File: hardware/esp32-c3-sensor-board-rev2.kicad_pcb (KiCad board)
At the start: 2 copper layers, 46 x 89 mm, 14 parts, among them J1 BME280_Module, J2 BH1750_Module, J3 Relay, J4 Button, J5 BREAKOUT, U1 ESP32-C3-SuperMini, U2 HLK-LD2410C

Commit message: Fix ESP32-C3 Super Mini pinout and re-route rev2
- Correct the U1 socket footprint pad order to match the physical module
  (pad 1 = 5V at the USB end, pad 8 = GPIO0, pad 9 = GPIO5, pad 16 = GPIO21).
- Use the reference pinout for I2C: SDA = GPIO8, SCL = GPIO9; free GPIO6/7
  go to the J5 breakout row. UART stays GPIO20/21, relay GPIO4, button GPIO3.
- Add full pin descriptions to the ESP32 symbol and board silkscreen
  (GPIOx plus MISO/MOSI/SS/SDA/SCL/RX/TX), and update all docs.
- Re-route the board against the corrected pin order (FreeRouting);
  DRC 0 errors / 0 unconnected, 2 pre-existing cosmetic silk warnings.
- Regenerate gerbers, drill, job file and the gerber zip.

doorbell.yml still lists GPIO6/7 for I2C and must be updated to
sda: GPIO8 / scl: GPIO9 on the software side.

Co-Authored-By: Claude Code <noreply@anthropic.com>
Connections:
- J5 pad 8: IO8 -> IO6
- J5 pad 9: IO9 -> IO7
- U1 pad 10: I2C_SDA -> IO6
- U1 pad 11: I2C_SCL -> IO7
- U1 pad 12: IO8 -> I2C_SDA
- U1 pad 13: IO9 -> I2C_SCL
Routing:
- net IO9: track 58.6 -> 0.00 mm
- net IO6: track 0.00 -> 52.1 mm
- net IO8: track 50.9 -> 0.00 mm
- net IO7: track 0.00 -> 49.9 mm, vias 0 -> 2
- net UART_RX: track 95.1 -> 62.2 mm, vias 0 -> 1
- net SPI_CS: track 86.1 -> 108.6 mm
- net I2C_SCL: track 71.7 -> 93.5 mm, vias 1 -> 0
- net 5V: track 67.6 -> 88.8 mm, vias 0 -> 1
- net IO0: track 34.6 -> 17.2 mm
- net UART_TX: track 74.5 -> 89.5 mm
- net 3V3: track 77.2 -> 90.9 mm
- net BUTTON: track 25.0 -> 36.8 mm
- net IO1: track 34.6 -> 24.1 mm
- net IO2: track 34.6 -> 27.3 mm, vias 0 -> 1
- net I2C_SDA: track 66.9 -> 73.3 mm, vias 1 -> 0
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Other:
- board text added: "GPIO0"
- board text added: "GPIO1"
- board text added: "GPIO10"
- board text added: "GPIO10 GPIO20=RX GPIO21=TX"
- board text added: "GPIO2"
- board text added: "GPIO20"
- board text added: "GPIO21"
- board text added: "GPIO4"
- board text added: "GPIO5"
- board text added: "GPIO6"
- board text added: "GPIO7"
- board text added: "GPIO7=SS GPIO8=SDA GPIO9=SCL"
- board text added: "GPIO8"
- board text added: "GPIO9"
- board text added: "JP1 1-2=I2C CSB->3V3 | 2-3=SPI CSB->GPIO5"
- board text added: "JP2 1-2=I2C 0x76 SDO->GND | 2-3=SPI MISO GPIO10"
- board text added: "U1 ALT: GPIO5=MISO GPIO6=MOSI"
- board text removed: "BTN"
- board text removed: "IO0"
- board text removed: "IO1"
- board text removed: "IO10"
- board text removed: "IO2"
- board text removed: "IO5"
- board text removed: "IO8"
- board text removed: "IO9"
- board text removed: "JP1 1-2=I2C CSB->3V3 | 2-3=SPI CSB->IO5"
- board text removed: "JP2 1-2=I2C 0x76 SDO->GND | 2-3=SPI MISO IO10"
- board text removed: "NC"
- board text removed: "RLY"

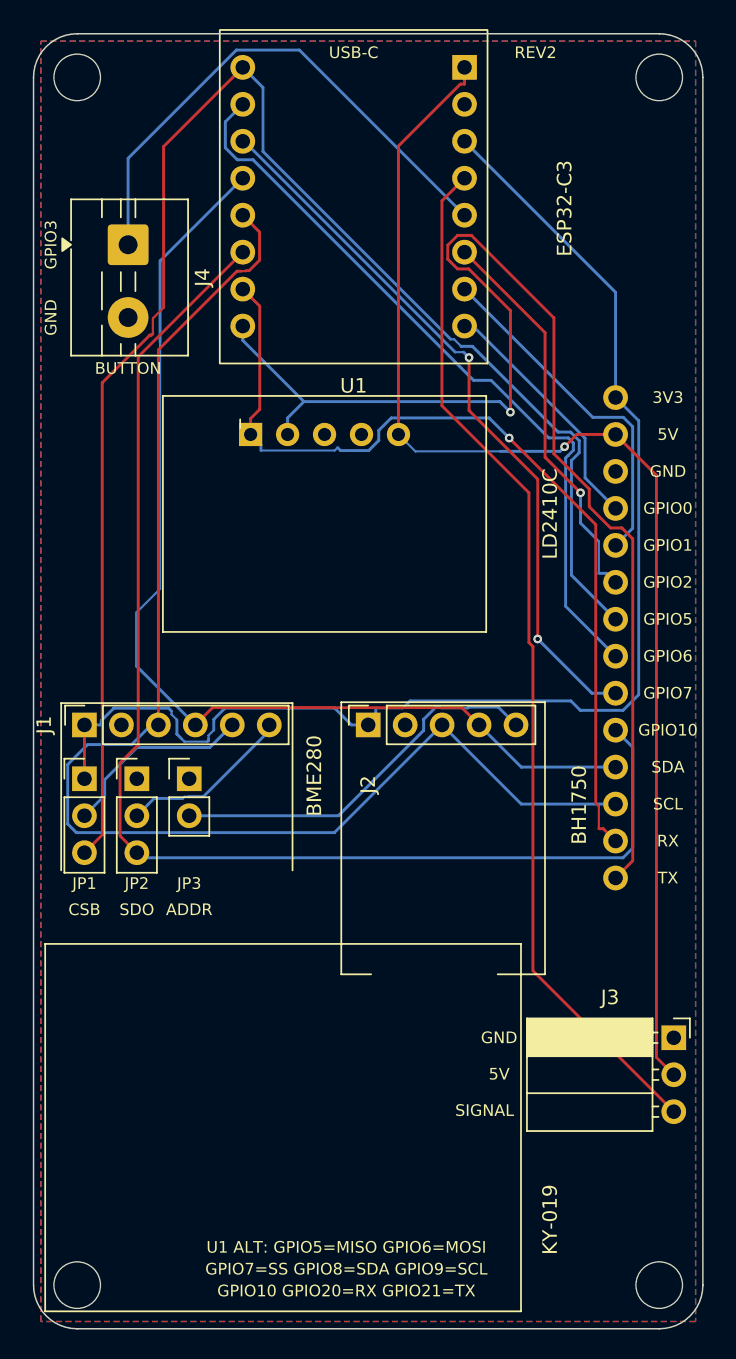
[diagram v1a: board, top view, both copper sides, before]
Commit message: Align BME280 SPI option with the ESP32-C3 reference pinout
- SPI_MISO moves from GPIO10 to GPIO5 (reference MISO)
- SPI_CS moves from GPIO5 to GPIO7 (reference SS)
- GPIO10 is now a free J5 breakout pin
- I2C stays SDA=GPIO8 / SCL=GPIO9; UART GPIO20/21; relay GPIO4; button GPIO3
- Re-route the affected nets; DRC 0 errors / 0 unconnected (2 cosmetic silk warnings)
- Update JP1/JP2 silkscreen legends and all pin-map docs
- Regenerate gerbers, drill, job file and gerber zip

The schematic symbol now maps: GPIO5/MISO->SPI_MISO, GPIO7/SS->SPI_CS,
GPIO8/SDA->I2C_SDA, GPIO9/SCL->I2C_SCL, GPIO20/RX->UART_RX, GPIO21/TX->UART_TX.
BME280 SPI mode reuses SCL/SDA as SCK/MOSI (GPIO9/GPIO8), since the module
shares those pins between I2C and SPI.

Co-Authored-By: Claude Code <noreply@anthropic.com>
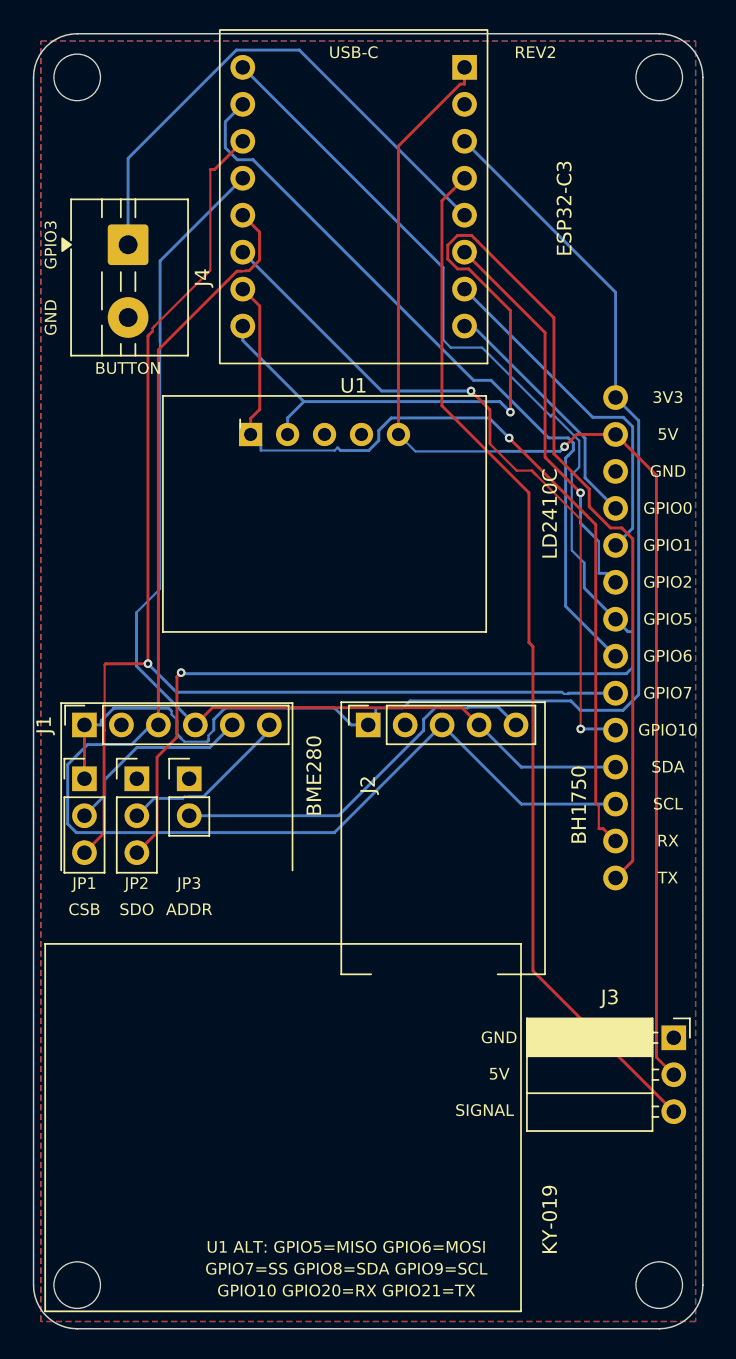
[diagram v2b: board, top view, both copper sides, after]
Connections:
- J5 pad 10: SPI_MISO -> IO10
- J5 pad 7: SPI_CS -> SPI_MISO
- J5 pad 9: IO7 -> SPI_CS
- U1 pad 11: IO7 -> SPI_CS
- U1 pad 14: SPI_MISO -> IO10
- U1 pad 9: SPI_CS -> SPI_MISO
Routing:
- net IO7: track 49.9 -> 0.00 mm, vias 2 -> 0
- net IO10: track 0.00 -> 49.0 mm, vias 0 -> 2
- net SPI_CS: track 108.6 -> 88.3 mm, vias 0 -> 1
- net SPI_MISO: track 88.3 -> 99.4 mm, vias 0 -> 1
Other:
- board text added: "JP1 1-2=I2C CSB->3V3 | 2-3=SPI CSB->GPIO7"
- board text added: "JP2 1-2=I2C 0x76 SDO->GND | 2-3=SPI MISO GPIO5"
- board text removed: "JP1 1-2=I2C CSB->3V3 | 2-3=SPI CSB->GPIO5"
- board text removed: "JP2 1-2=I2C 0x76 SDO->GND | 2-3=SPI MISO GPIO10"
